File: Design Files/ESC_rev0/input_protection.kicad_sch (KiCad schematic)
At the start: 13 parts, among them U3 XT30PW-M, U4 XH-2PWBPZ

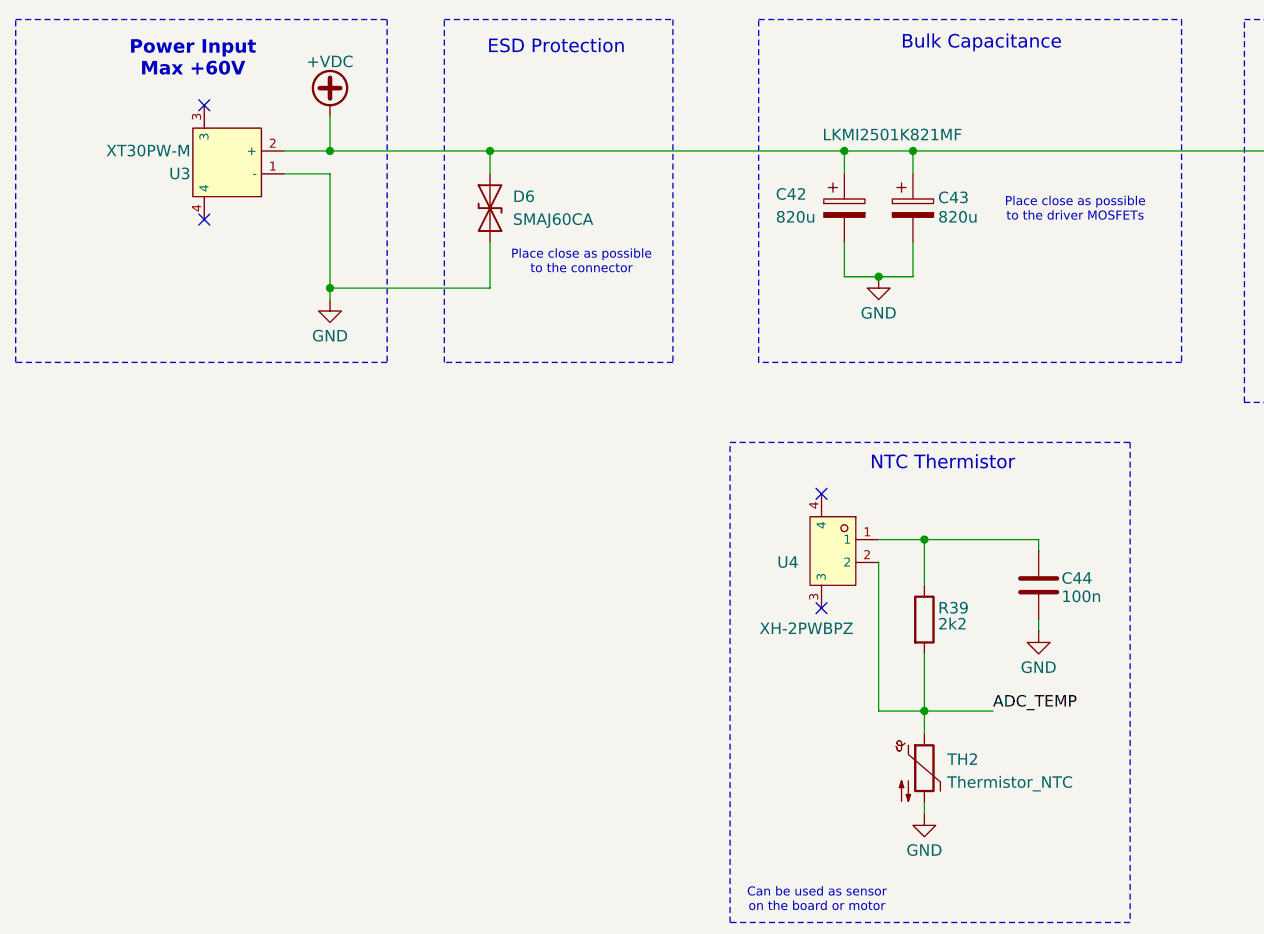
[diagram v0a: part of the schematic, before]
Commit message: update10
modifications to root page, completion of pages step_down and mechanical
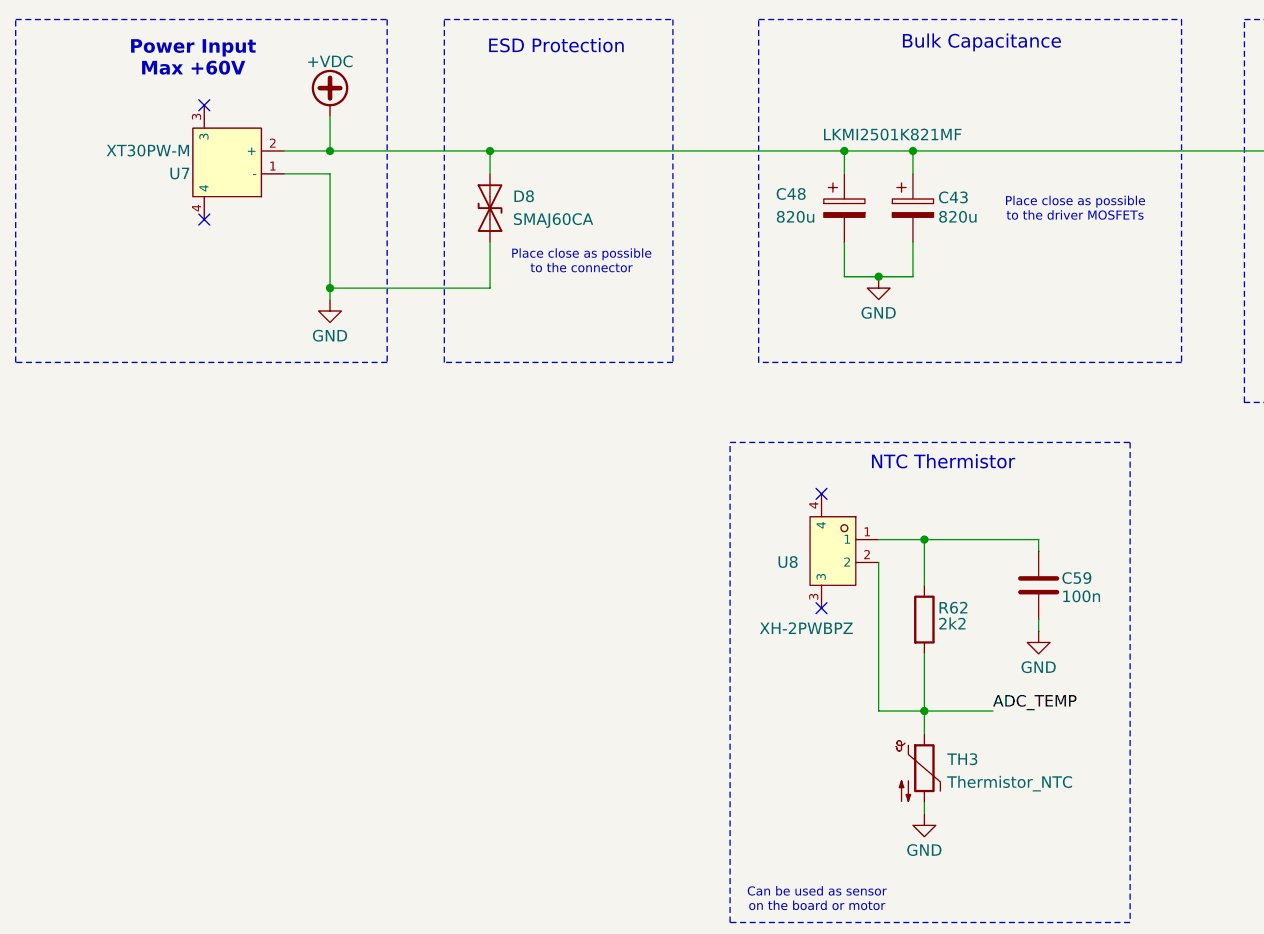
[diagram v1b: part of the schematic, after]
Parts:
- renumbered C42 to C48, C44 to C59, D6 to D8, R39 to R62, TH2 to TH3, U3 to U7, U4 to U8
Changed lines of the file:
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@@
 		(on_board yes)
 		(dnp no)
-		(property "Reference" "U3"
+		(property "Reference" "U7"
 			(at 48.006 64.77 90)
 			(effects
@@
 		(pin "3"
 		)
-		(instances
-			(project ""
-				(path "/7906e740-34c4-4b06-b70f-1daa08872946/3e80544b-2d3b-437c-8c9a-22b201e65208"
-					(reference "U3")
-					(unit 1)
-				)
-			)
-		)
 	)
 	(symbol
@@
 		(dnp no)
 		(fields_autoplaced yes)
-		(property "Reference" "TH2"
+		(property "Reference" "TH3"
 			(at 132.08 129.8574 0)
 			(effects
@@
 		)
 		(pin "1"
-		)
-		(instances
-			(project ""
-				(path "/7906e740-34c4-4b06-b70f-1daa08872946/3e80544b-2d3b-437c-8c9a-22b201e65208"
-					(reference "TH2")
-					(unit 1)
-				)
-			)
 		)
 	)
@@
 		(on_board yes)
 		(dnp no)
-		(property "Reference" "#PWR051"
+		(property "Reference" "#PWR086"
 			(at 63.5 85.09 0)
 			(effects
@@
 		)
 		(pin "1"
-		)
-		(instances
-			(project ""
-				(path "/7906e740-34c4-4b06-b70f-1daa08872946/3e80544b-2d3b-437c-8c9a-22b201e65208"
-					(reference "#PWR051")
-					(unit 1)
-				)
-			)
 		)
 	)
@@
 		(on_board yes)
 		(dnp no)
-		(property "Reference" "U4"
+		(property "Reference" "U8"
 			(at 115.57 107.9501 0)
 			(effects
@@
 		)
 		(pin "4"
-		)
-		(instances
-			(project ""
-				(path "/7906e740-34c4-4b06-b70f-1daa08872946/3e80544b-2d3b-437c-8c9a-22b201e65208"
-					(reference "U4")
-					(unit 1)
-				)
-			)
 		)
 	)
@@
 		(on_board yes)
 		(dnp no)
-		(property "Reference" "#PWR050"
+		(property "Reference" "#PWR082"
 			(at 63.5 60.96 0)
 			(effects
@@
 		)
 		(pin "1"
-		)
-		(instances
-			(project ""
-				(path "/7906e740-34c4-4b06-b70f-1daa08872946/3e80544b-2d3b-437c-8c9a-22b201e65208"
-					(reference "#PWR050")
-					(unit 1)
-				)
-			)
 		)
 	)
@@
 		(on_board yes)
 		(dnp no)
-		(property "Reference" "R39"
+		(property "Reference" "R62"
 			(at 131.064 113.03 0)
 			(effects
@@
 		(pin "2"
 		)
-		(instances
-			(project ""
-				(path "/7906e740-34c4-4b06-b70f-1daa08872946/3e80544b-2d3b-437c-8c9a-22b201e65208"
-					(reference "R39")
-					(unit 1)
-				)
-			)
-		)
 	)
 	(symbol
@@
 		(on_board yes)
 		(dnp no)
-		(property "Reference" "C42"
+		(property "Reference" "C48"
 			(at 113.03 67.056 0)
 			(effects
@@
 		(pin "1"
 		)
-		(instances
-			(project ""
-				(path "/7906e740-34c4-4b06-b70f-1daa08872946/3e80544b-2d3b-437c-8c9a-22b201e65208"
-					(reference "C42")
-					(unit 1)
-				)
-			)
-		)
 	)
 	(symbol
@@
 		(dnp no)
 		(fields_autoplaced yes)
-		(property "Reference" "D6"
+		(property "Reference" "D8"
 			(at 83.82 67.3099 90)
 			(effects
@@
 		)
 		(pin "2"
-		)
-		(instances
-			(project ""
-				(path "/7906e740-34c4-4b06-b70f-1daa08872946/3e80544b-2d3b-437c-8c9a-22b201e65208"
-					(reference "D6")
-					(unit 1)
-				)
-			)
 		)
 	)
@@
 		(on_board yes)
 		(dnp no)
-		(property "Reference" "C44"
+		(property "Reference" "C59"
 			(at 144.78 109.728 0)
 			(effects
@@
 		(pin "1"
 		)
-		(instances
-			(project ""
-				(path "/7906e740-34c4-4b06-b70f-1daa08872946/3e80544b-2d3b-437c-8c9a-22b201e65208"
-					(reference "C44")
-					(unit 1)
-				)
-			)
-		)
-	)
+	)

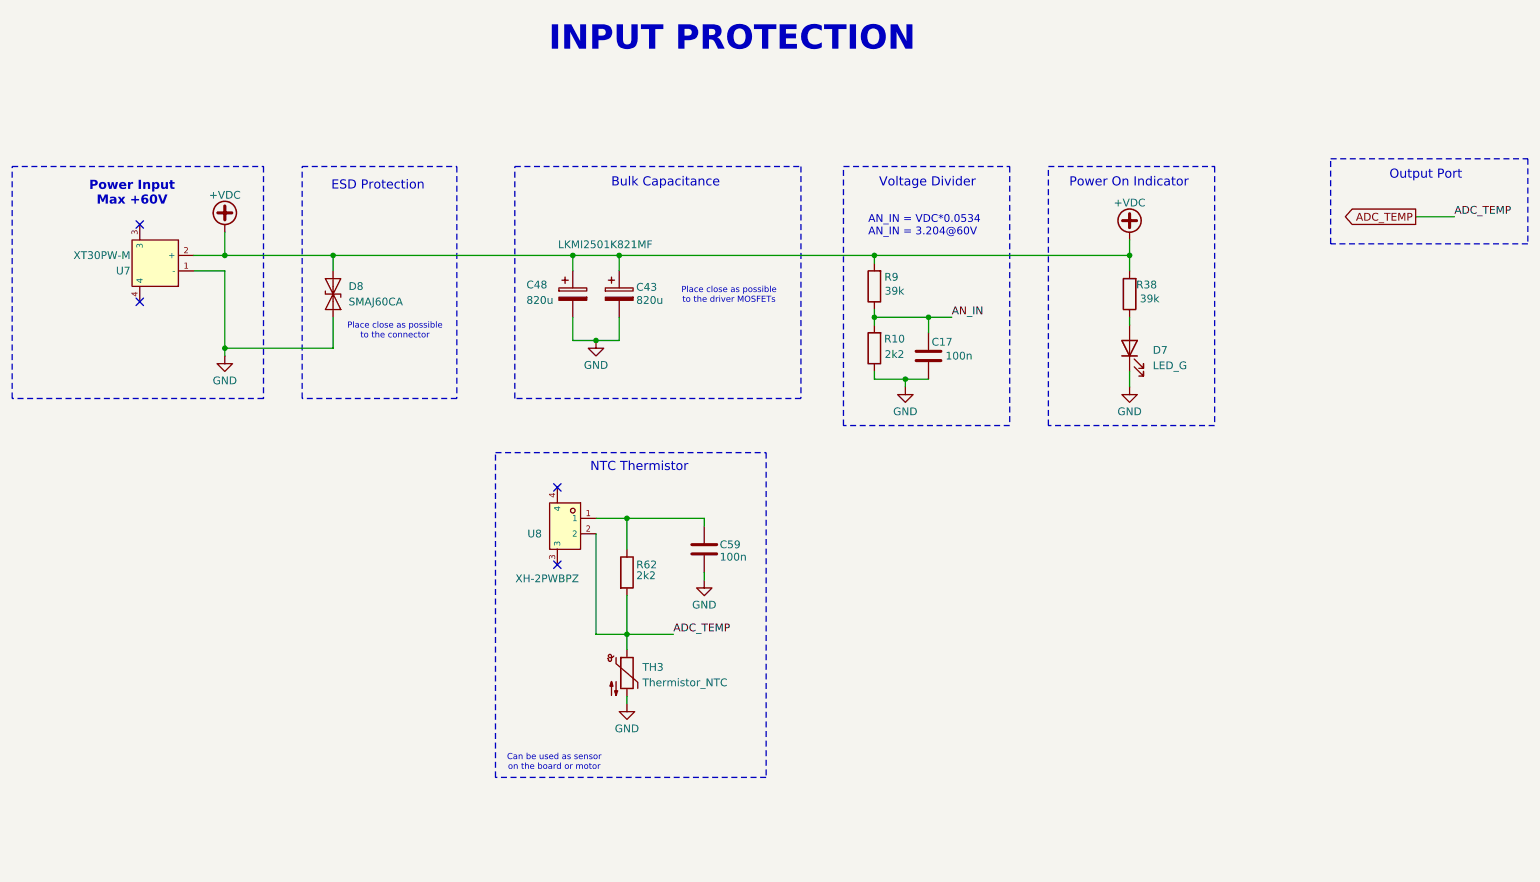
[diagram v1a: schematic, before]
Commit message: UPDATE 12
started schematics revision: edit and added info and circuits to some pages and assigned some footprints for components
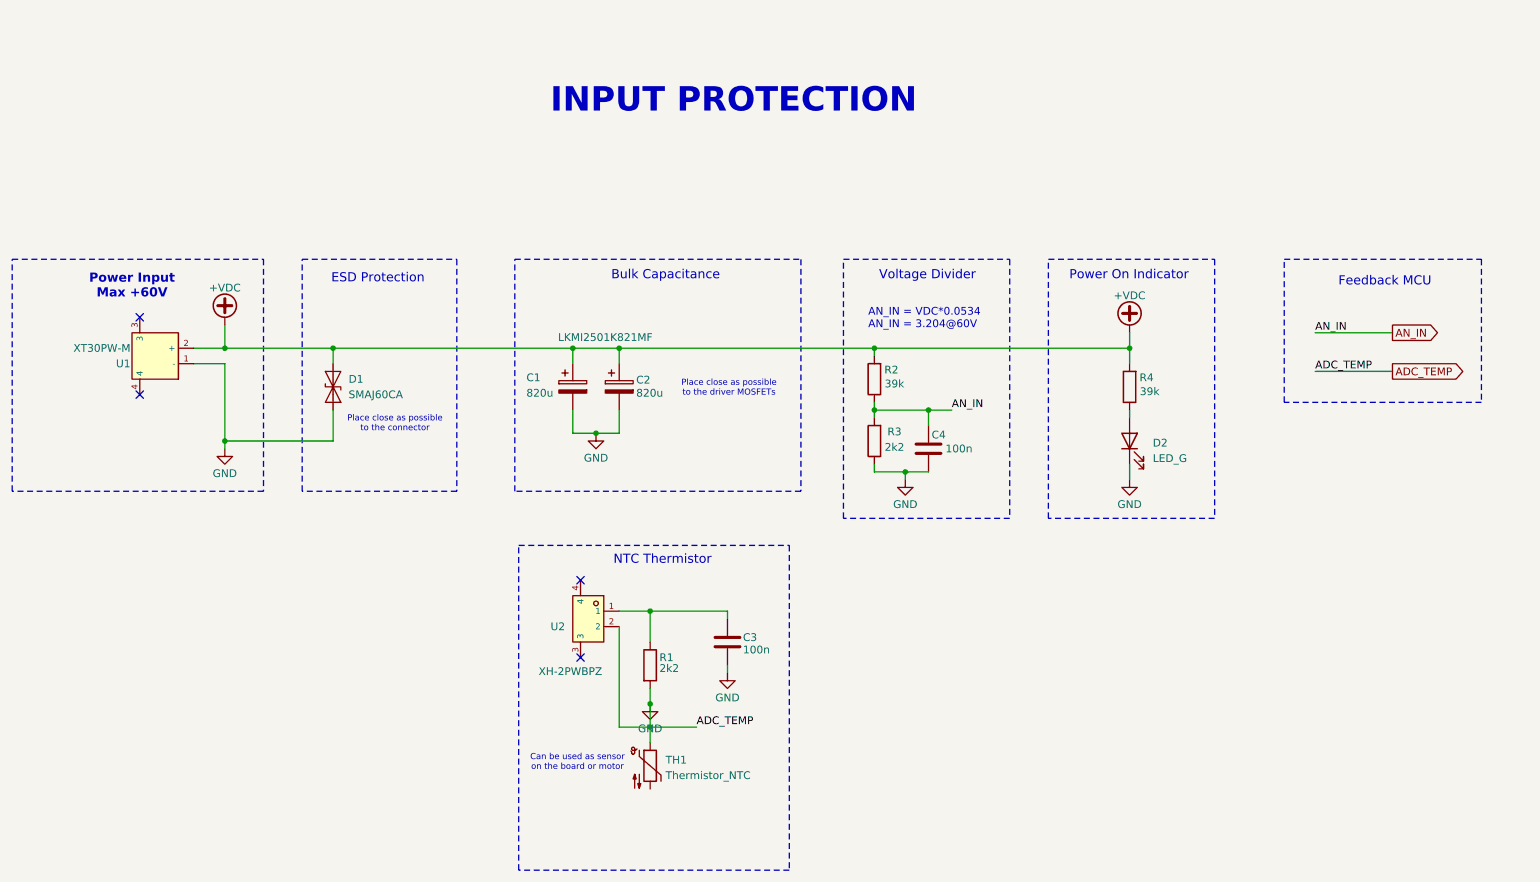
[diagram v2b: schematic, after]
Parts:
- C3: renamed from C59; footprint (none) -> Capacitor_SMD:C_0201_0603Metric
- C4: renamed from C17; footprint (none) -> Capacitor_SMD:C_0201_0603Metric
- D2: renamed from D7; footprint (none) -> LED_SMD:LED_0201_0603Metric
- renumbered C48 to C1, C43 to C2, D8 to D1, R62 to R1, R9 to R2, R10 to R3, R38 to R4, TH3 to TH1, U7 to U1, U8 to U2
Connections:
- net ADC_TEMP is gone; now on net GND: R1.2, TH1.1, U2.2
- net GND: no longer TH1.2
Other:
- note added: "Feedback MCU"
- note removed: "Output Port"
- moved on the sheet: C1, C2, C3, C4, D1, D2, R1, R2, R3, R4, TH1, U1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

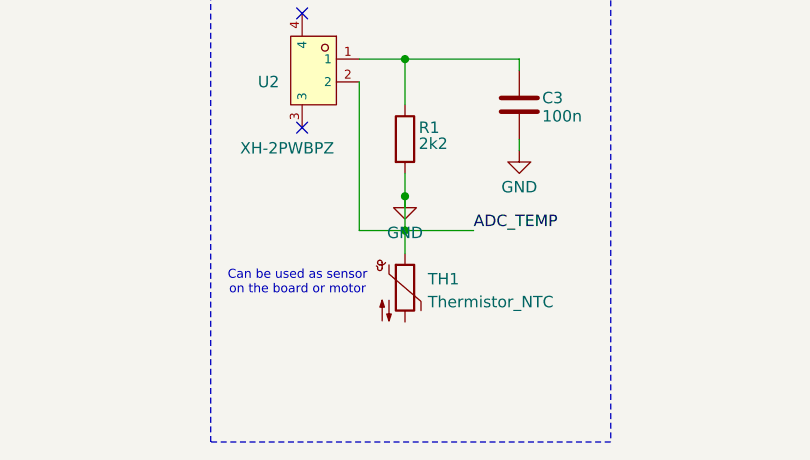
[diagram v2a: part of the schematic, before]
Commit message: update 13
assigned all footprints (provisionally) and imported them - errors and warning occurred, must be corrected in the future
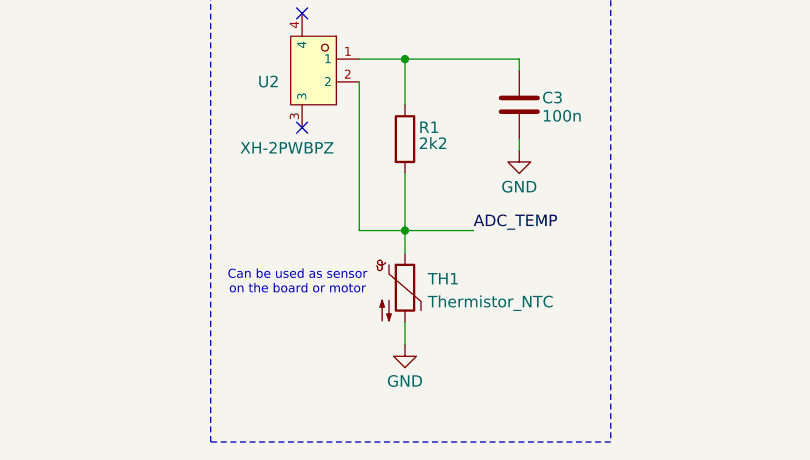
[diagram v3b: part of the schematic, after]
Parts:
- R1, R2, R3, R4: footprint (none) -> Resistor_SMD:R_0603_1608Metric
- TH1: footprint (none) -> Capacitor_THT:C_Radial_D4.0mm_H5.0mm_P1.50mm
- U1: footprint footprint:CONN-TH_XT30PW-M -> Connector_AMASS:AMASS_XT30PW-M_1x02_P2.50mm_Horizontal
- U2: footprint footprint:CONN-SMD_XH-2PWBPZ -> XH-2PWBPZ_foot:CONN-SMD_XH-2PWBPZ
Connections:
- net GND: now also TH1.2; no longer R1.2, TH1.1, U2.2
- new net ADC_TEMP: R1.2, TH1.1, U2.2
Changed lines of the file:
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@@
-	)
-	(junction
-		(at 133.35 135.89)
-		(diameter 0)
-		(color 0 0 0 0)
 	)
 	(junction
@@
 	(wire
 		(pts
-			(xy 133.35 139.7) (xy 133.35 135.89)
+			(xy 133.35 149.86) (xy 133.35 152.4)
+		)
+		(stroke
+			(width 0)
+			(type default)
+		)
+	)
+	(wire
+		(pts
+			(xy 133.35 133.35) (xy 133.35 139.7)
 		)
 		(stroke
@@
 		(pts
 			(xy 212.09 96.52) (xy 212.09 99.06)
-		)
-		(stroke
-			(width 0)
-			(type default)
-		)
-	)
-	(wire
-		(pts
-			(xy 133.35 133.35) (xy 133.35 135.89)
 		)
 		(stroke
@@
 			)
 		)
-		(property "Footprint" "footprint:CONN-TH_XT30PW-M"
+		(property "Footprint" "Connector_AMASS:AMASS_XT30PW-M_1x02_P2.50mm_Horizontal"
 			(at 43.18 78.74 0)
 			(effects
@@
 			)
 		)
-		(property "Footprint" ""
+		(property "Footprint" "Capacitor_THT:C_Radial_D4.0mm_H5.0mm_P1.50mm"
 			(at 133.35 144.78 0)
 			(effects
@@
 			)
 		)
-		(property "Footprint" ""
+		(property "Footprint" "Resistor_SMD:R_0603_1608Metric"
 			(at 171.958 92.71 90)
 			(effects
@@
 			)
 		)
-		(property "Footprint" "footprint:CONN-SMD_XH-2PWBPZ"
+		(property "Footprint" "XH-2PWBPZ_foot:CONN-SMD_XH-2PWBPZ"
 			(at 124.46 132.08 0)
 			(effects
@@
 	(symbol
 		(lib_id "power:GND")
-		(at 133.35 135.89 0)
+		(at 133.35 152.4 0)
 		(unit 1)
 		(exclude_from_sim no)
@@
 		(dnp no)
 		(property "Reference" "#PWR04"
-			(at 133.35 142.24 0)
+			(at 133.35 158.75 0)
 			(effects
 				(font
@@
 		)
 		(property "Value" "GND"
-			(at 133.35 139.954 0)
+			(at 133.35 156.464 0)
 			(effects
 				(font
@@
 		)
 		(property "Footprint" ""
-			(at 133.35 135.89 0)
+			(at 133.35 152.4 0)
 			(effects
 				(font
@@
 		)
 		(property "Datasheet" ""
-			(at 133.35 135.89 0)
+			(at 133.35 152.4 0)
 			(effects
 				(font
@@
 		)
 		(property "Description" "Power symbol creates a global label with name \"GND\" , ground"
-			(at 133.35 135.89 0)
+			(at 133.35 152.4 0)
 			(effects
 				(font
@@
 			)
 		)
-		(property "Footprint" ""
+		(property "Footprint" "Resistor_SMD:R_0603_1608Metric"
 			(at 131.572 129.54 90)
 			(effects
@@
 			)
 		)
-		(property "Footprint" ""
+		(property "Footprint" "Resistor_SMD:R_0603_1608Metric"
 			(at 171.958 82.55 90)
 			(effects
@@
 			)
 		)
-		(property "Footprint" ""
+		(property "Footprint" "Resistor_SMD:R_0603_1608Metric"
 			(at 213.868 83.82 90)
 			(effects
